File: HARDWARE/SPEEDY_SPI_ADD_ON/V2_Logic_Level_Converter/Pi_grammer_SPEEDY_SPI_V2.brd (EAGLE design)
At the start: 22.9 x 61 mm, 11 parts, among them J2 TARGET_copy

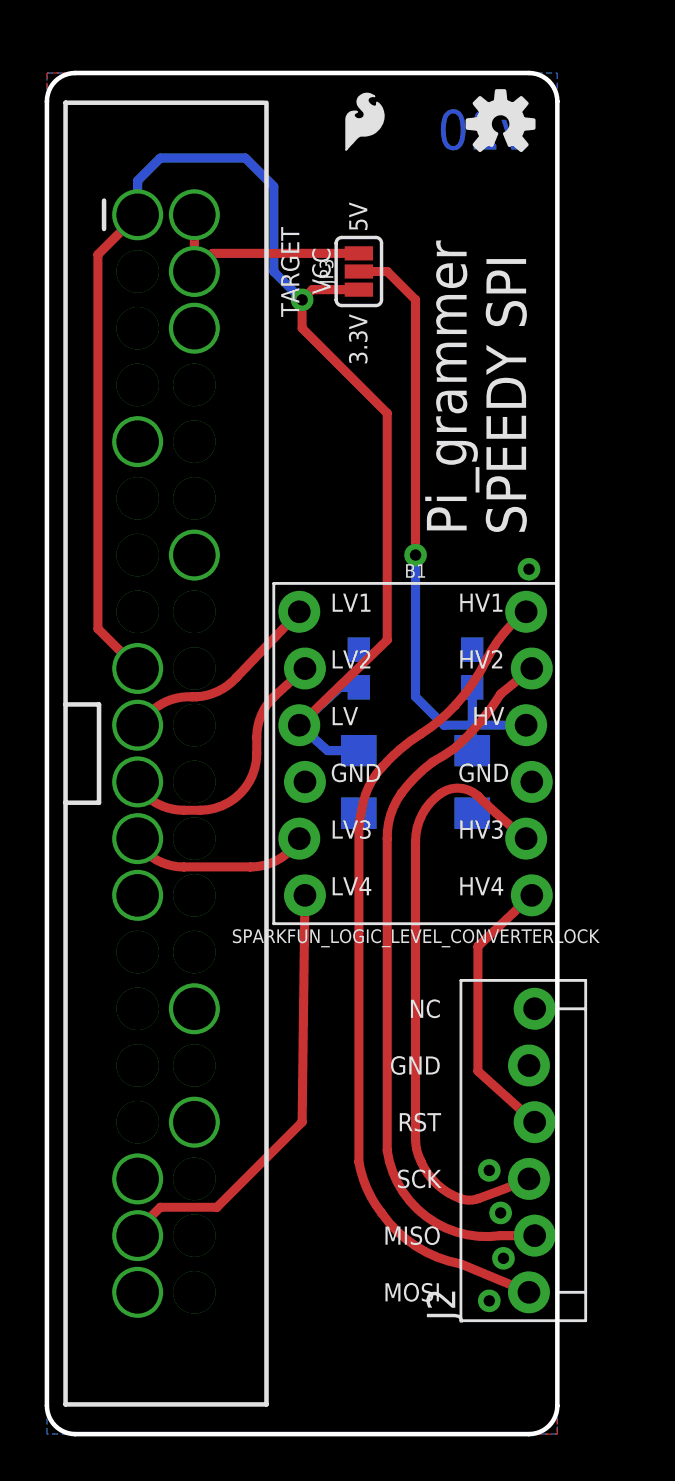
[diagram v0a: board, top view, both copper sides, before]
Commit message: Option to "tap" logic level from target
Note, this required a modification to the ADAPTER as well. I am
utilizing pin 6 on the 1x6 pin header (jumper wire) to transfer VCC back
to the logic level converter.

I'm not sure why on the original design I didn't think to include VCC in
the comm lines to the target - I think it was because the raspi doesn't
have any ADCs to actually  verify it, so I didn't know if it was worth
it.
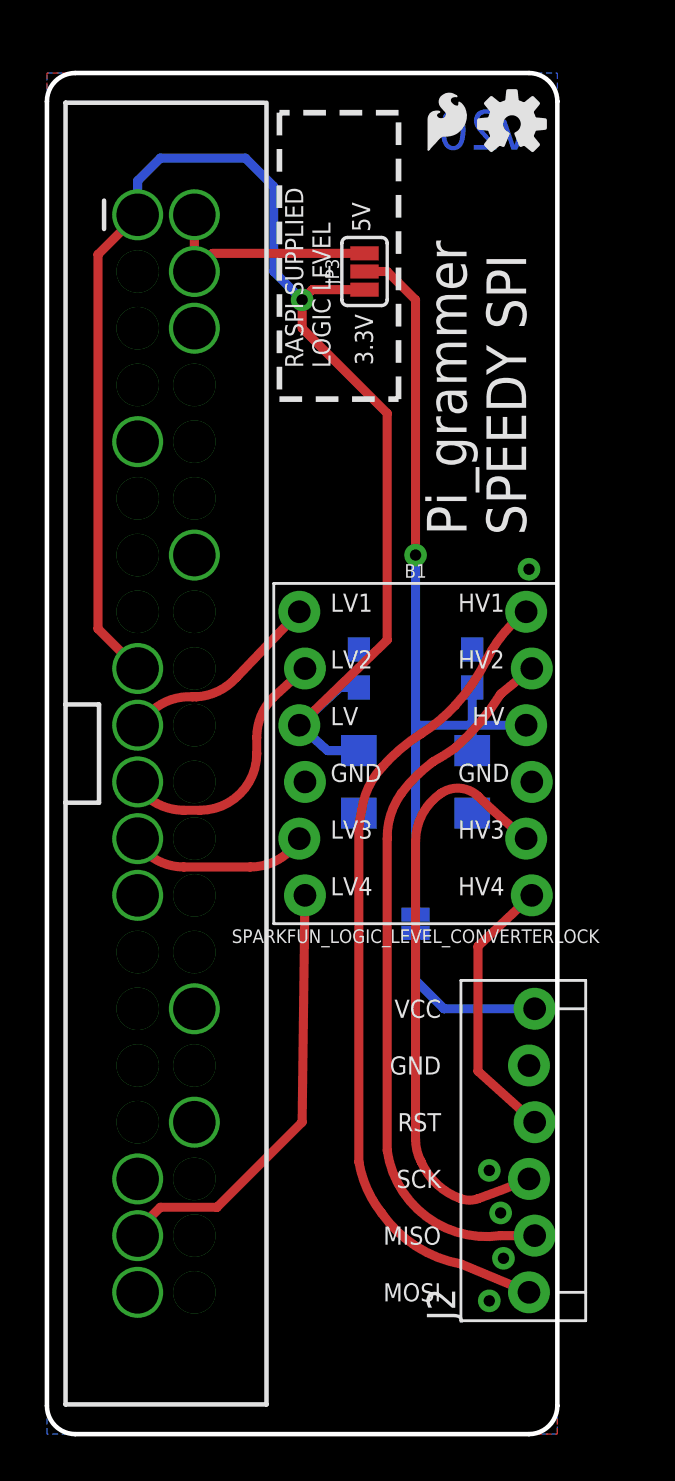
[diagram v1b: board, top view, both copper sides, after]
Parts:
- added JP1: VCC_Target, SparkFun-Jumpers:SMT-JUMPER_2_NO_SILK
- moved LOGO1 3.68 mm to (61.2, 72.4)
- moved LOGO2 0.51 mm to (65.3, 73.9)
- moved JP3 0.25 mm to (58.7, 67.3)
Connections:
- new net VCC_T: J2.6, JP1.2
- net N$4: now also JP1.1
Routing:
- net N$4: track 29.2 -> 38.1 mm
- net VCC_T: track 0.00 -> 7.99 mm
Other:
- board text added: "RASPI SUPPLIED LOGIC LEVEL"
- board text added: "TARGET SUPPLIED LOGIC LEVEL"
- board text removed: "TARGET"
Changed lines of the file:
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@@
 <layer number="39" name="tKeepout" color="4" fill="11" visible="no" active="yes"/>
 <layer number="40" name="bKeepout" color="1" fill="11" visible="no" active="yes"/>
-<layer number="41" name="tRestrict" color="4" fill="10" visible="yes" active="yes"/>
-<layer number="42" name="bRestrict" color="1" fill="10" visible="yes" active="yes"/>
+<layer number="41" name="tRestrict" color="4" fill="10" visible="no" active="yes"/>
+<layer number="42" name="bRestrict" color="1" fill="10" visible="no" active="yes"/>
 <layer number="43" name="vRestrict" color="2" fill="10" visible="no" active="yes"/>
 <layer number="44" name="Drills" color="7" fill="1" visible="no" active="yes"/>
@@
 <wire x1="36.83" y1="21.59" x2="39.37" y2="21.59" width="0.2032" layer="49"/>
 <wire x1="33.02" y1="24.13" x2="33.02" y2="19.685" width="0.254" layer="49"/>
-<text x="55.753" y="65.278" size="0.8128" layer="21" font="vector" ratio="15" rot="R90">TARGET</text>
-<text x="57.15" y="66.294" size="0.8128" layer="21" font="vector" ratio="15" rot="R90">VCC</text>
-<text x="58.801" y="69.088" size="0.8128" layer="21" font="vector" ratio="15" rot="R90">5V</text>
-<text x="58.801" y="63.119" size="0.8128" layer="21" font="vector" ratio="15" rot="R90">3.3V</text>
+<text x="57.15" y="62.992" size="0.8128" layer="21" font="vector" ratio="15" rot="R90">RASPI SUPPLIED
+LOGIC LEVEL</text>
+<text x="58.928" y="69.088" size="0.8128" layer="21" font="vector" ratio="15" rot="R90">5V</text>
+<text x="59.055" y="63.119" size="0.8128" layer="21" font="vector" ratio="15" rot="R90">3.3V</text>
 <wire x1="67.31" y1="74.93" x2="67.31" y2="16.51" width="0.2032" layer="20"/>
 <wire x1="67.31" y1="16.51" x2="66.04" y2="15.24" width="0.2032" layer="20" curve="-90"/>
@@
 <text x="62.103" y="29.21" size="0.8128" layer="21" font="vector" ratio="15" align="center-right">RST</text>
 <text x="62.103" y="31.75" size="0.8128" layer="21" font="vector" ratio="15" align="center-right">GND</text>
-<text x="62.103" y="34.29" size="0.8128" layer="21" font="vector" ratio="15" align="center-right">NC</text>
+<text x="62.103" y="34.29" size="0.8128" layer="21" font="vector" ratio="15" align="center-right">VCC</text>
 <text x="65.913" y="55.499" size="1.778" layer="21" font="vector" ratio="15" rot="R90">Pi_grammer
 SPEEDY SPI</text>
+<text x="61.976" y="36.449" size="0.8128" layer="22" font="vector" ratio="15" rot="MR270">TARGET SUPPLIED
+LOGIC LEVEL</text>
+<wire x1="62.865" y1="40.386" x2="62.865" y2="23.368" width="0.254" layer="22" style="shortdash"/>
+<wire x1="62.865" y1="23.368" x2="58.674" y2="23.368" width="0.254" layer="22" style="shortdash"/>
+<wire x1="58.674" y1="23.368" x2="58.674" y2="40.386" width="0.254" layer="22" style="shortdash"/>
+<wire x1="58.674" y1="40.386" x2="62.865" y2="40.386" width="0.254" layer="22" style="shortdash"/>
+<wire x1="60.198" y1="61.595" x2="60.198" y2="74.422" width="0.254" layer="21" style="shortdash"/>
+<wire x1="60.198" y1="74.422" x2="54.864" y2="74.422" width="0.254" layer="21" style="shortdash"/>
+<wire x1="54.864" y1="74.422" x2="54.864" y2="61.595" width="0.254" layer="21" style="shortdash"/>
+<wire x1="54.864" y1="61.595" x2="60.198" y2="61.595" width="0.254" layer="21" style="shortdash"/>
 </plain>
 <attributes>
@@
 <elements>
 <element name="JP2" library="SparkFun-Boards" package="2X20-SHROUDED-SOLDER-ON-TOP" value="RASPBERRYPI-B+-GPIOSOLDER-ON-TOP" x="49.784" y="45.72"/>
-<element name="LOGO1" library="SparkFun-Aesthetics" package="SFE_LOGO_FLAME_.1" value="SFE_LOGO_FLAME.1_INCH" x="57.531" y="72.39"/>
-<element name="LOGO2" library="SparkFun-Aesthetics" package="OSHW-LOGO-S" value="OSHW-LOGOS" x="64.77" y="73.914"/>
+<element name="LOGO1" library="SparkFun-Aesthetics" package="SFE_LOGO_FLAME_.1" value="SFE_LOGO_FLAME.1_INCH" x="61.214" y="72.39"/>
+<element name="LOGO2" library="SparkFun-Aesthetics" package="OSHW-LOGO-S" value="OSHW-LOGOS" x="65.278" y="73.914"/>
 <element name="J2" library="SparkFun-Connectors" package="MOLEX-1X6_LOCK" value="TARGET_copy" x="66.04" y="21.59" rot="R90">
 <attribute name="PROD_ID" value="CONN-09698" x="66.04" y="21.59" size="1.778" layer="27" rot="R90" display="off"/>
@@
 <element name="FRAME1" library="SparkFun-Aesthetics" package="CREATIVE_COMMONS" value="FRAME-LETTER" x="21.59" y="-21.59"/>
 <element name="B1" library="SparkFun-Boards" package="SPARKFUN_LOGIC_LEVEL_CONVERTER_LOCK" value="SPARKFUN_LOGIC_LEVEL_CONVERTERLOCK" x="60.96" y="45.72"/>
-<element name="JP3" library="SparkFun-Jumpers" package="SMT-JUMPER_3_NO_SILK" value="Target Logic Select" x="58.42" y="67.31" rot="R90"/>
+<element name="JP3" library="SparkFun-Jumpers" package="SMT-JUMPER_3_NO_SILK" value="Target Logic Select" x="58.674" y="67.31" rot="R90"/>
 <element name="C3" library="SparkFun-Capacitors" package="0603" value="0.1uF" x="58.42" y="49.53" rot="MR90">
 <attribute name="PROD_ID" value="CAP-00810" x="58.42" y="49.53" size="1.778" layer="28" font="vector" ratio="15" rot="MR90" display="off"/>
@@
 <attribute name="PROD_ID" value="CAP-00811" x="58.42" y="44.45" size="1.778" layer="28" font="vector" ratio="15" rot="MR90" display="off"/>
 </element>
+<element name="JP1" library="SparkFun-Jumpers" package="SMT-JUMPER_2_NO_SILK" value="VCC_Target" x="60.96" y="38.1" rot="MR270"/>
 </elements>
 <signals>
@@
 <contactref element="JP3" pad="3"/>
 <wire x1="51.054" y1="67.31" x2="51.8668" y2="68.1228" width="0.4064" layer="1"/>
-<wire x1="51.8668" y1="68.1228" x2="58.42" y2="68.1228" width="0.4064" layer="1"/>
+<wire x1="51.8668" y1="68.1228" x2="58.674" y2="68.1228" width="0.4064" layer="1"/>
 <wire x1="51.054" y1="67.31" x2="51.054" y2="69.85" width="0.4064" layer="1"/>
 <contactref element="JP2" pad="4"/>
@@
 <via x="55.88" y="66.04" extent="1-16" drill="0.508" diameter="1.016"/>
 <wire x1="55.88" y1="66.04" x2="56.3372" y2="66.4972" width="0.4064" layer="1"/>
-<wire x1="56.3372" y1="66.4972" x2="58.42" y2="66.4972" width="0.4064" layer="1"/>
+<wire x1="56.3372" y1="66.4972" x2="58.674" y2="66.4972" width="0.4064" layer="1"/>
 <wire x1="58.42" y1="45.85" x2="57.02" y2="45.85" width="0.4064" layer="16"/>
 <wire x1="57.02" y1="45.85" x2="55.753" y2="46.99" width="0.4064" layer="16"/>
@@
 <contactref element="B1" pad="HV"/>
 <contactref element="JP3" pad="2"/>
-<wire x1="58.42" y1="67.31" x2="59.69" y2="67.31" width="0.4064" layer="1"/>
+<wire x1="58.674" y1="67.31" x2="59.69" y2="67.31" width="0.4064" layer="1"/>
 <wire x1="59.69" y1="67.31" x2="60.96" y2="66.04" width="0.4064" layer="1"/>
 <wire x1="60.96" y1="66.04" x2="60.96" y2="54.61" width="0.4064" layer="1"/>
@@
 <contactref element="C4" pad="1"/>
 <via x="60.96" y="54.61" extent="1-16" drill="0.508" diameter="1.016"/>
-<wire x1="60.96" y1="54.61" x2="60.96" y2="48.26" width="0.4064" layer="16"/>
-<wire x1="60.96" y1="48.26" x2="62.23" y2="46.99" width="0.4064" layer="16"/>
-<wire x1="62.23" y1="46.99" x2="63.5" y2="46.99" width="0.4064" layer="16"/>
 <wire x1="63.5" y1="46.99" x2="65.913" y2="46.99" width="0.4064" layer="16"/>
 <wire x1="63.5" y1="45.85" x2="63.5" y2="46.99" width="0.4064" layer="16"/>
 <wire x1="63.5" y1="48.68" x2="63.5" y2="46.99" width="0.4064" layer="16"/>
+<contactref element="JP1" pad="1"/>
+<wire x1="60.96" y1="38.5064" x2="60.96" y2="46.99" width="0.4064" layer="16"/>
+<wire x1="60.96" y1="46.99" x2="60.96" y2="54.61" width="0.4064" layer="16"/>
+<wire x1="63.5" y1="46.99" x2="60.96" y2="46.99" width="0.4064" layer="16"/>
+</signal>
+<signal name="VCC_T">
+<contactref element="J2" pad="6"/>
+<contactref element="JP1" pad="2"/>
+<wire x1="66.294" y1="34.29" x2="62.23" y2="34.29" width="0.4064" layer="16"/>
+<wire x1="62.23" y1="34.29" x2="60.96" y2="35.56" width="0.4064" layer="16"/>
+<wire x1="60.96" y1="35.56" x2="60.96" y2="37.6936" width="0.4064" layer="16"/>
 </signal>
 </signals>
